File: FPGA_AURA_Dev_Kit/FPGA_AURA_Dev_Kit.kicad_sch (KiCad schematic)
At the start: 11 parts, among them J1 Barrel_Jack, J2 Conn_Coaxial_Small, J3 Conn_Coaxial_Small, J4 AVR-JTAG-10, J5 Conn_02x10_Odd_Even, J6 Conn_02x10_Odd_Even

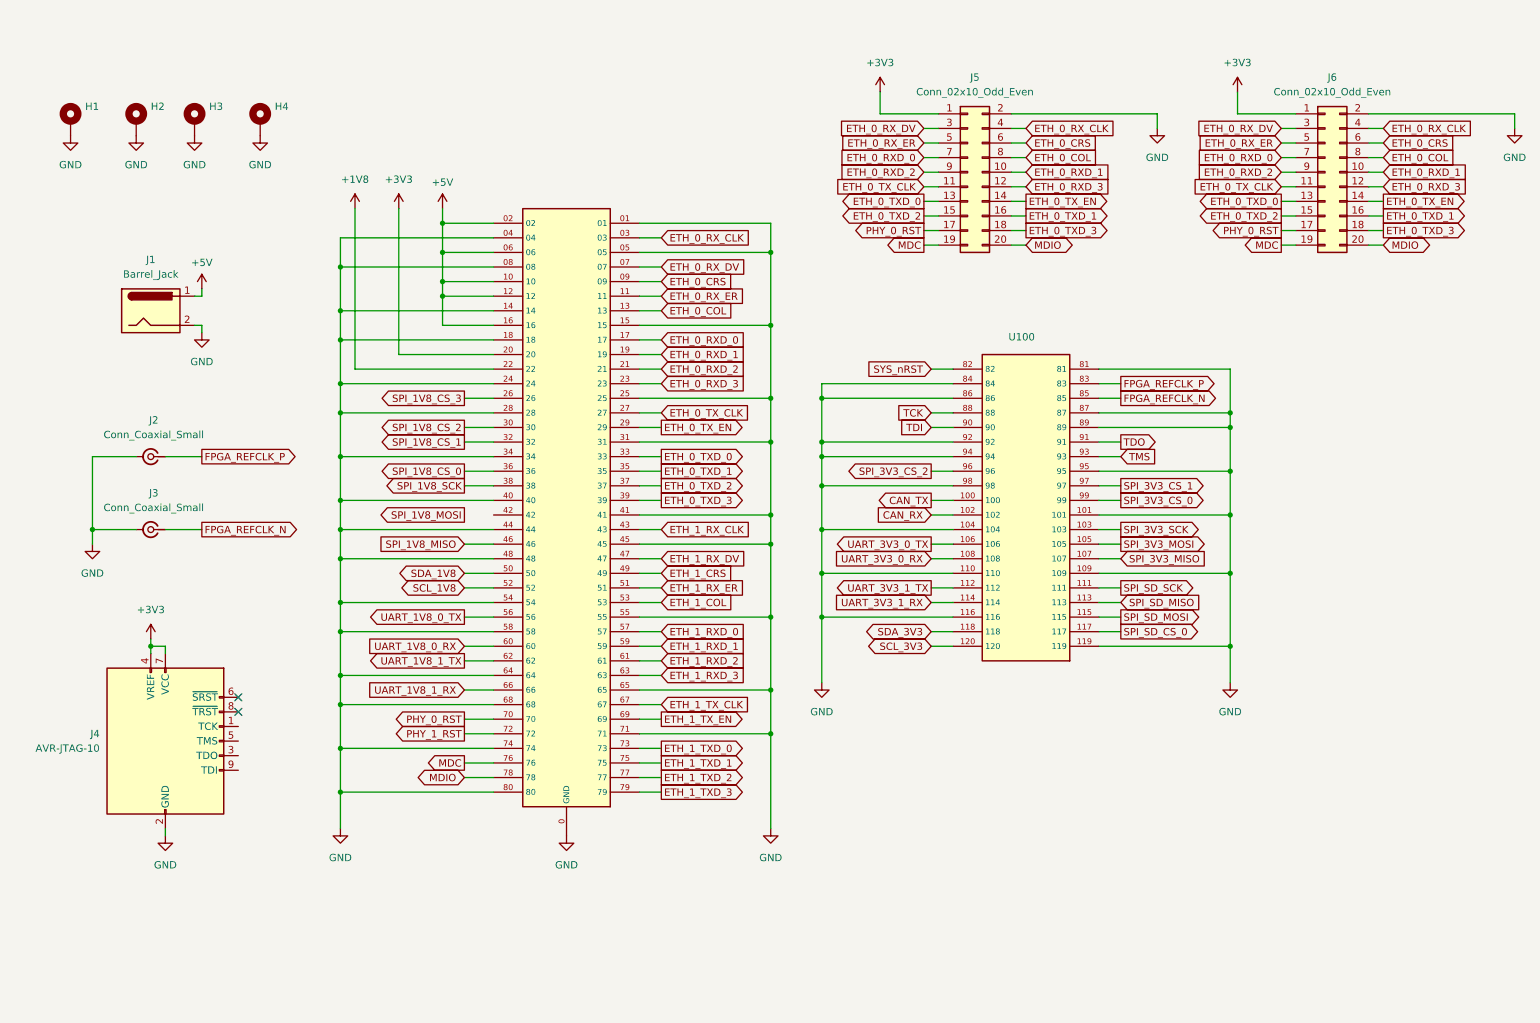
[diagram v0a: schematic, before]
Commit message: Continued dev kit. Moving focus to ordering FPGA prior to finishing dev kit.
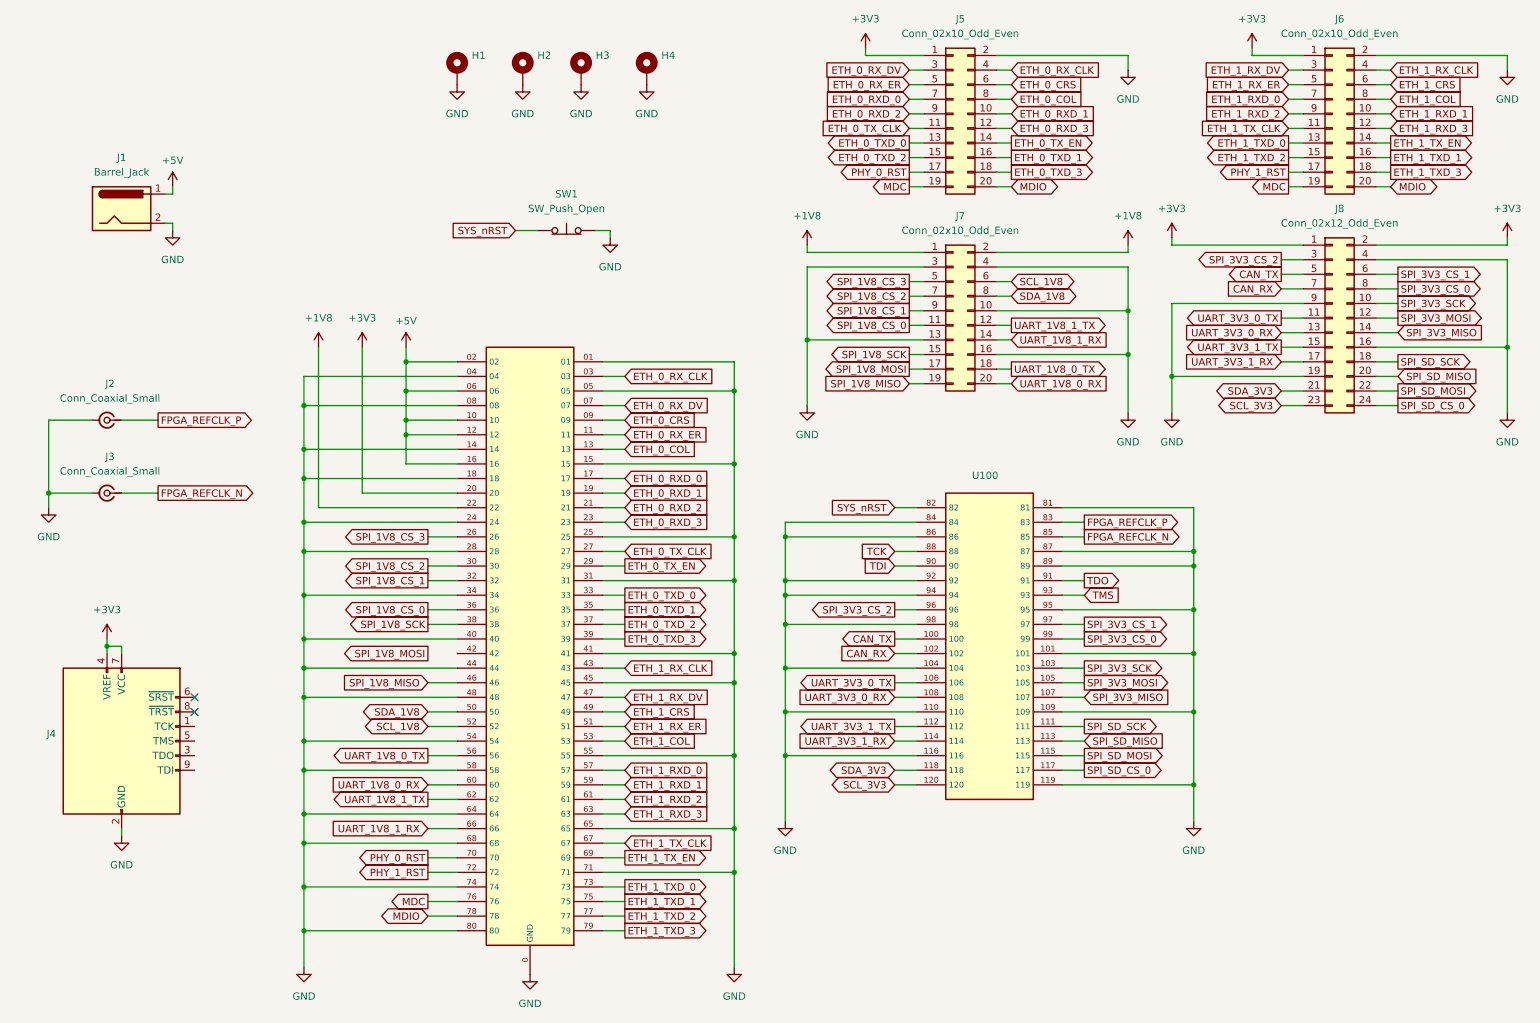
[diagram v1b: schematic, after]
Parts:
- added J7: Conn_02x10_Odd_Even, Connector_PinHeader_2.54mm:PinHeader_2x10_P2.54mm_Vertical, symbol Connector_Generic:Conn_02x10_Odd_Even
- added J8: Conn_02x12_Odd_Even, Connector_PinHeader_2.54mm:PinHeader_2x12_P2.54mm_Vertical, symbol Connector_Generic:Conn_02x12_Odd_Even
- added SW1: SW_Push_Open, Button_Switch_SMD:SW_SPST_CK_RS282G05A3, symbol Switch:SW_Push_Open
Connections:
- net +1V8: now also J7.1 (Pin_1), J7.2 (Pin_2)
- net +3V3: now also J8.1 (Pin_1), J8.2 (Pin_2)
- net CAN_RX: now also J8.7 (Pin_7)
- net CAN_TX: now also J8.5 (Pin_5)
- net ETH_0_COL: no longer J6.8 (Pin_8)
- net ETH_0_CRS: no longer J6.6 (Pin_6)
- net ETH_0_RXD_0: no longer J6.7 (Pin_7)
- net ETH_0_RXD_1: no longer J6.10 (Pin_10)
- net ETH_0_RXD_2: no longer J6.9 (Pin_9)
- net ETH_0_RXD_3: no longer J6.12 (Pin_12)
- net ETH_0_RX_CLK: no longer J6.4 (Pin_4)
- net ETH_0_RX_DV: no longer J6.3 (Pin_3)
- net ETH_0_RX_ER: no longer J6.5 (Pin_5)
- net ETH_0_TXD_0: no longer J6.13 (Pin_13)
- net ETH_0_TXD_1: no longer J6.16 (Pin_16)
- net ETH_0_TXD_2: no longer J6.15 (Pin_15)
- net ETH_0_TXD_3: no longer J6.18 (Pin_18)
- net ETH_0_TX_CLK: no longer J6.11 (Pin_11)
- net ETH_0_TX_EN: no longer J6.14 (Pin_14)
- net ETH_1_COL: now also J6.8 (Pin_8)
- net ETH_1_CRS: now also J6.6 (Pin_6)
- net ETH_1_RXD_0: now also J6.7 (Pin_7)
- net ETH_1_RXD_1: now also J6.10 (Pin_10)
- net ETH_1_RXD_2: now also J6.9 (Pin_9)
- net ETH_1_RXD_3: now also J6.12 (Pin_12)
- net ETH_1_RX_CLK: now also J6.4 (Pin_4)
- net ETH_1_RX_DV: now also J6.3 (Pin_3)
- net ETH_1_RX_ER: now also J6.5 (Pin_5)
- net ETH_1_TXD_0: now also J6.13 (Pin_13)
- net ETH_1_TXD_1: now also J6.16 (Pin_16)
- net ETH_1_TXD_2: now also J6.15 (Pin_15)
- net ETH_1_TXD_3: now also J6.18 (Pin_18)
- net ETH_1_TX_CLK: now also J6.11 (Pin_11)
- net ETH_1_TX_EN: now also J6.14 (Pin_14)
- net GND: now also J7.10 (Pin_10), J7.13 (Pin_13), J7.16 (Pin_16), J7.3 (Pin_3), J7.4 (Pin_4), J8.16 (Pin_16), J8.19 (Pin_19), J8.4 (Pin_4), J8.9 (Pin_9), SW1.2 (B)
- net PHY_0_RST: no longer J6.17 (Pin_17)
- net PHY_1_RST: now also J6.17 (Pin_17)
- net SCL_1V8: now also J7.6 (Pin_6)
- net SCL_3V3: now also J8.23 (Pin_23)
- net SDA_1V8: now also J7.8 (Pin_8)
- net SDA_3V3: now also J8.21 (Pin_21)
- net SPI_1V8_CS_0: now also J7.11 (Pin_11)
- net SPI_1V8_CS_1: now also J7.9 (Pin_9)
- net SPI_1V8_CS_2: now also J7.7 (Pin_7)
- net SPI_1V8_CS_3: now also J7.5 (Pin_5)
- net SPI_1V8_MISO: now also J7.19 (Pin_19)
- net SPI_1V8_MOSI: now also J7.17 (Pin_17)
- net SPI_1V8_SCK: now also J7.15 (Pin_15)
- net SPI_3V3_CS_0: now also J8.8 (Pin_8)
- net SPI_3V3_CS_1: now also J8.6 (Pin_6)
- net SPI_3V3_CS_2: now also J8.3 (Pin_3)
- net SPI_3V3_MISO: now also J8.14 (Pin_14)
- net SPI_3V3_MOSI: now also J8.12 (Pin_12)
- net SPI_3V3_SCK: now also J8.10 (Pin_10)
- net SPI_SD_CS_0: now also J8.24 (Pin_24)
- net SPI_SD_MISO: now also J8.20 (Pin_20)
- net SPI_SD_MOSI: now also J8.22 (Pin_22)
- net SPI_SD_SCK: now also J8.18 (Pin_18)
- net SYS_nRST: now also SW1.1 (A)
- net UART_1V8_0_RX: now also J7.20 (Pin_20)
- net UART_1V8_0_TX: now also J7.18 (Pin_18)
- net UART_1V8_1_RX: now also J7.14 (Pin_14)
- net UART_1V8_1_TX: now also J7.12 (Pin_12)
- net UART_3V3_0_RX: now also J8.13 (Pin_13)
- net UART_3V3_0_TX: now also J8.11 (Pin_11)
- net UART_3V3_1_RX: now also J8.17 (Pin_17)
- net UART_3V3_1_TX: now also J8.15 (Pin_15)
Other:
- company: (none) -> Alexander Armitage
- title: (none) -> AURA FPGA Dev Kit
- moved on the sheet: H1, H2, H3, H4, J1, J2, J3, J4, J5, J6, U100
